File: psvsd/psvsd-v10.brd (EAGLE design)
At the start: 30 x 33.2 mm, 30 parts, among them J1 MEM2051-00-195-00, U1 USB2244QFN, U3 VREG, Y1 24.000MHz

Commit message: Removed old LDO and reset circuit. Added new power efficient POR circuit & dual channel LDO
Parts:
- added C16: 1uF, rcl:C0603
- added C17: 1nF, rcl:C0402
- added C18: 0.1uF, resistor:C0402
- added C19: 0.1uF, rcl:C0402
- added D1: 3.3V, diode:SOD523
- added U2: 74AUP1G74DC, NXP_60_26022015:SOT765
- C2: value 10uF -> 1uF
- R2: value 165K -> 100K
- U3: value VREG -> LP3996_DSC_10; device v-reg-micrel:SOT23-5 -> LP3996:SDA10A
- moved U3 52.5 mm to (-22.1, -15.0), flipped to the top, turned to 0 degrees
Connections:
- net VDD18PLL renamed USBVDD18PLL
- new net N$2: C19.1, D1.A, R3.1, U2.7
- new net N$4: C17.1, U3.4
- new net N$5: C18.1, U3.5
- new net ONSWA: U$1.25, U2.1
- new net PSHOLD: U$1.15, U2.2, U2.3, U3.3
- new net USBVDD18: C8.1, U1.13
- net !RESET: now also U3.8; no longer R3.2
- net GND: now also C16.2, C17.2, C18.2, C19.2, U2.4, U3.11, U3.6; no longer R2.1, U3.2
- net VDD18: now also C16.1, D1.C, R3.2, U2.6, U2.8, U3.10; no longer C8.1, U1.13
- net VDD33: now also R2.1, U3.9; no longer U3.5
- net VDD5: now also U3.2; no longer R3.1, U3.3
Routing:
- net VDD5: track 27.6 -> 13.1 mm
- net VDD33: track 55.5 -> 49.6 mm
- net !RESET: track 6.28 -> 1.15 mm
- net VDD18: track 2.23 -> 0.00 mm
- net USBVDD18: track 0.00 -> 2.23 mm

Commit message: Layout for PM circuit
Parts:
- moved C17 74.0 mm to (6.10, 27.9), flipped to the bottom, turned to 90 degrees
- moved C18 61.7 mm to (7.62, 27.9), flipped to the bottom, turned to 90 degrees
- moved D1 60.6 mm to (13.7, 13.2), flipped to the bottom, turned to 270 degrees
- moved C19 57.3 mm to (16.5, 11.2), flipped to the bottom, turned to 180 degrees
- moved U3 50.1 mm to (8.89, 24.4), flipped to the bottom, turned to 180 degrees
- moved C16 41.1 mm to (12.7, 25.4), flipped to the bottom, turned to 90 degrees
- moved U2 9.94 mm to (13.7, 10.2)
- moved R3 2.01 mm to (12.1, 14.0), turned to 90 degrees
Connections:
- net N$2 renamed !S
- net N$4 renamed CBYP
- net N$5 renamed CSET
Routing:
- net PSHOLD: track 0.00 -> 29.5 mm, vias 0 -> 1
- net VDD18: track 0.00 -> 24.1 mm, vias 0 -> 2
- net !RESET: track 1.15 -> 16.2 mm, vias 0 -> 2
- net VDD33: track 49.6 -> 64.4 mm
- net VDD5: track 13.1 -> 25.4 mm
- net ONSWA: track 0.00 -> 9.09 mm, vias 0 -> 1
- net !S: track 0.00 -> 5.60 mm
- net CBYP: track 0.00 -> 3.22 mm
- net CSET: track 0.00 -> 2.63 mm
- net VDD: track 26.8 -> 28.1 mm, vias 1 -> 3
- net GND: track 2.00 -> 2.02 mm, vias 26 -> 23

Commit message: Changed to cheaper molex slot
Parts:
- removed J1: MEM2051-00-195-00, sd-mmc:MEM2051
- added U$2: MOLEX-47219-2001, molex:MOLEX:47219-2001
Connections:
- removed net !CD: J1.9, U1.26
- net GND: now also U$2.P6, U1.26; no longer J1.6
- net SD_CLK: now also U$2.P5; no longer J1.5
- net SD_CMD: now also U$2.P3; no longer J1.3
- net SD_D0: now also U$2.P7; no longer J1.7
- net SD_D1: now also U$2.P8; no longer J1.8
- net SD_D2: now also U$2.P1; no longer J1.1
- net SD_D3: now also U$2.P2; no longer J1.2
- net VDD: now also U$2.P4; no longer J1.4
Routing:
- net !CD: track 12.4 -> 0.00 mm, vias 1 -> 0
- net VDD33: track 64.4 -> 52.9 mm, vias 2 -> 1
- net VDD18: track 24.1 -> 26.8 mm
- net GND: track 2.02 -> 0.26 mm, vias 23 -> 20
- net SD_D0: track 7.69 -> 9.04 mm
- net SD_CLK: track 12.4 -> 13.6 mm
- net SD_CMD: track 13.2 -> 14.1 mm

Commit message: Routed new layout
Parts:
- turned C6 to 180 degrees
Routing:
- net GND: track 0.26 -> 8.05 mm, vias 20 -> 24
- net VDD33: track 52.9 -> 60.1 mm, vias 1 -> 3
- net !RESET: track 16.2 -> 18.7 mm
- net VDD: track 27.9 -> 26.6 mm
- net +5V: track 1.86 -> 2.40 mm

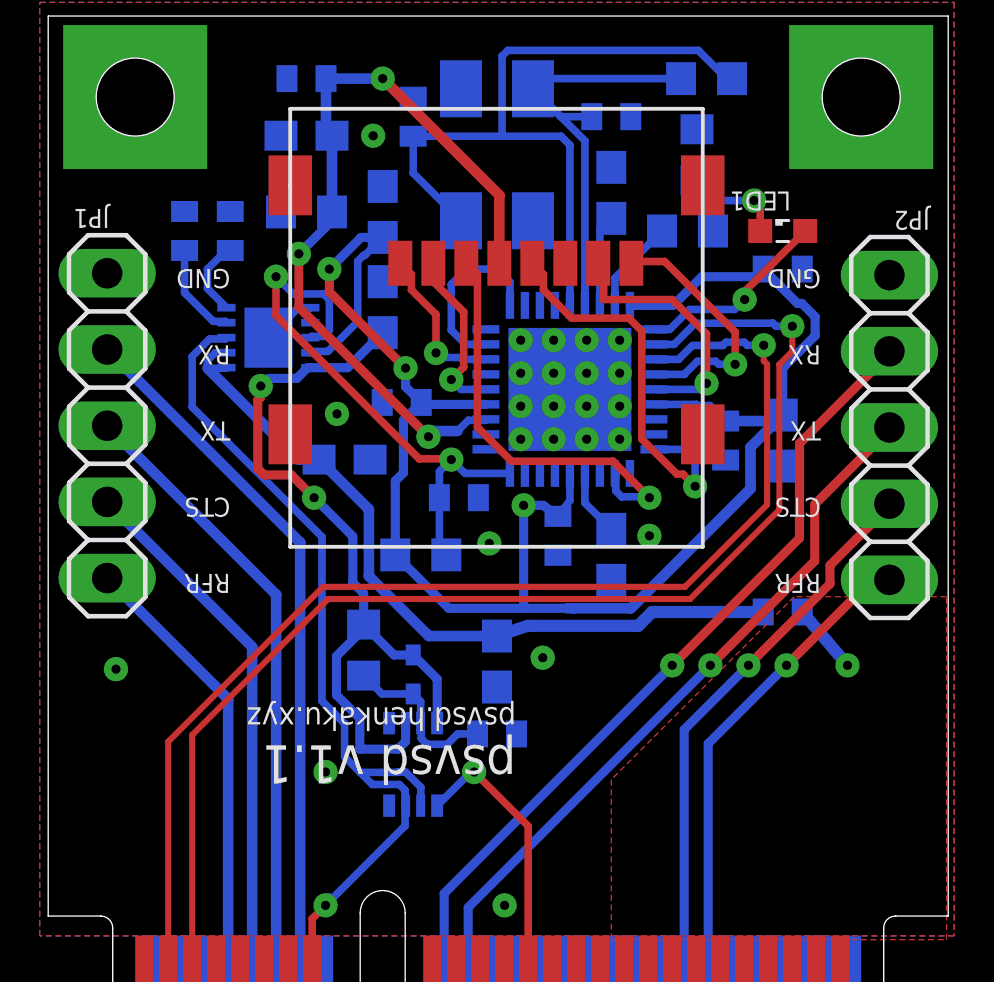
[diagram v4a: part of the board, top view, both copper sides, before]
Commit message: Placed labels for new components
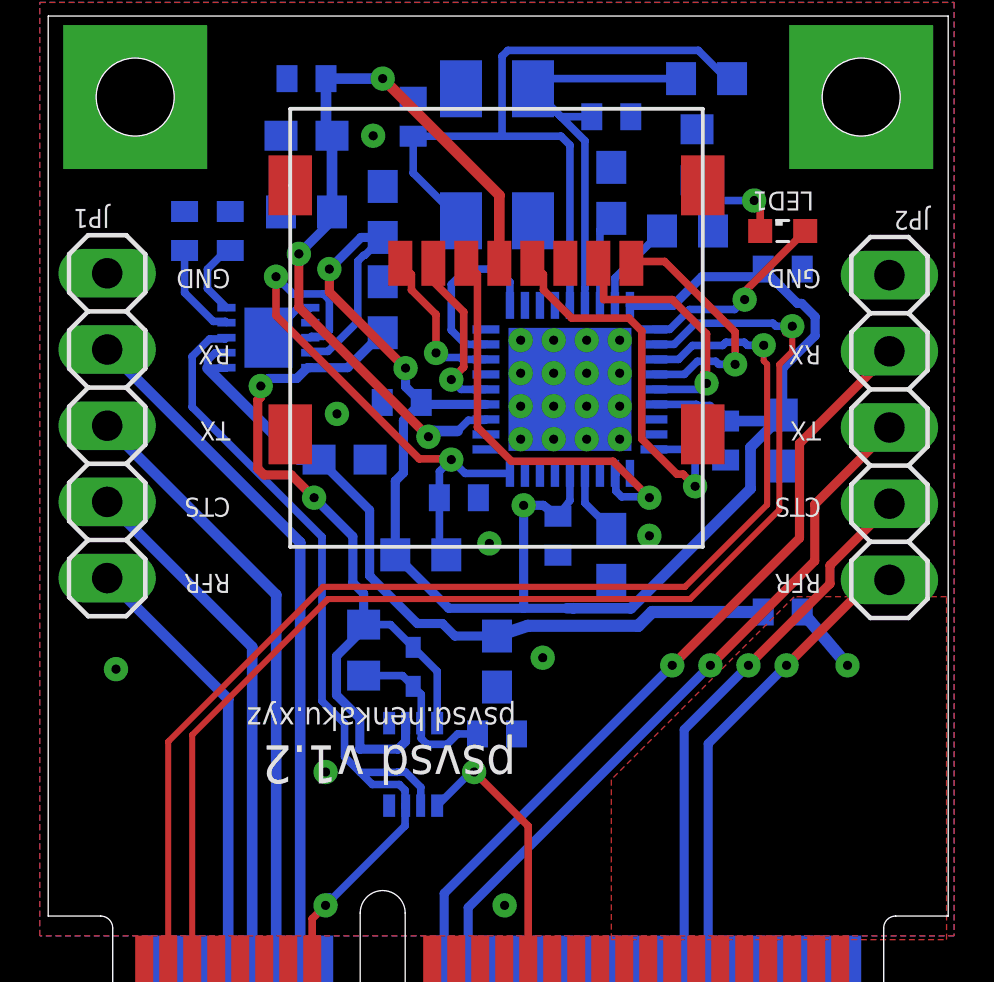
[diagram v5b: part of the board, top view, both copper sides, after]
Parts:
- moved D1 0.25 mm to (13.7, 13.5)
- renumbered U$2 to SD1
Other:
- board text added: "psvsd v1.2"
- board text removed: "psvsd v1.1"
